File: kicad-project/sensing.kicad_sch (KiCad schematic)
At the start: 10 parts

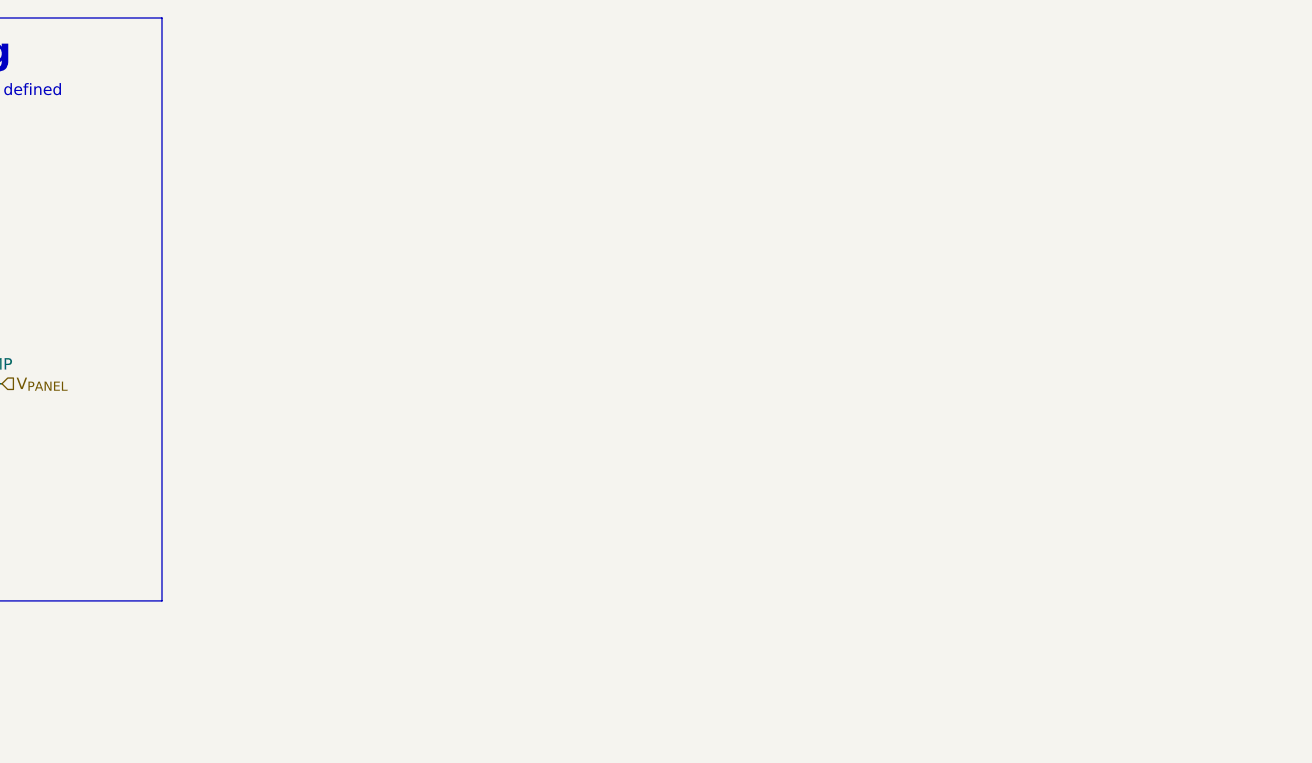
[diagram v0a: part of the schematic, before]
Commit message: fw: added MPU9250
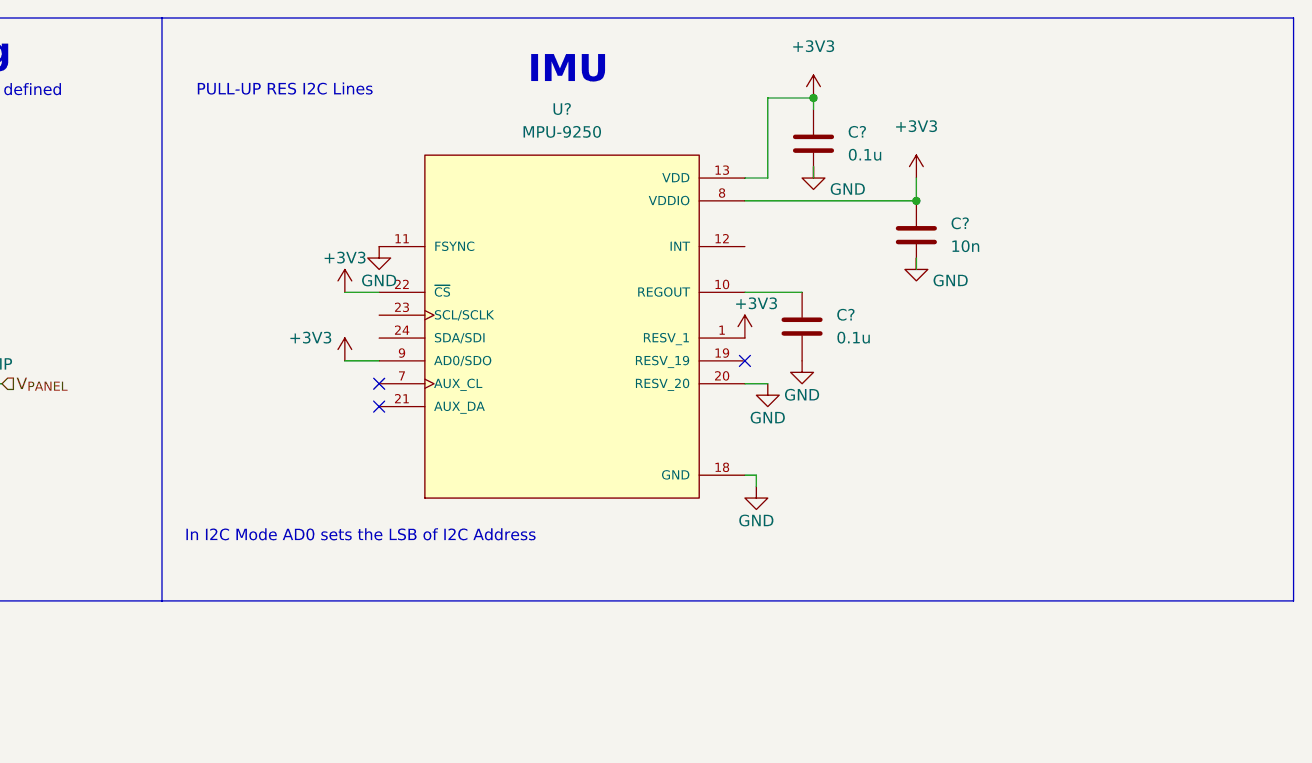
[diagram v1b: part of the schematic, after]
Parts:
- added C? (x2): 0.1u, symbol Device:C
- added C?: 10n, symbol Device:C
- added U?: MPU-9250, QFN40P300X300X105-24N, symbol MPU-9250:MPU-9250
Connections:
- net +3V3: now also C?.1, C?.1, U?.1 (RESV_1), U?.13 (VDD), U?.22 (~{CS}), U?.8 (VDDIO), U?.9 (AD0/SDO)
- net GND: now also C?.2, C?.2, C?.2, U?.11 (FSYNC), U?.18 (GND), U?.20 (RESV_20)
- new net: C?.1, U?.10 (REGOUT)
- no-connect marks 0 -> 3
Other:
- note added: "IMU"
- note added: "In I2C Mode AD0 sets the LSB of I2C Address"
- note added: "PULL-UP RES I2C Lines"

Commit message: hw: add limit switches, dual power input, actuation sheet, debug and expansion connectors and connect sheets
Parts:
- added J? (x2): Conn_01x03, symbol Connector_Generic:Conn_01x03
- C? (x2): value 0.1u -> 100n
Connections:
- net +3V3: now also J?.1 (Pin_1), J?.1 (Pin_1)
- net GND: now also J?.3 (Pin_3), J?.3 (Pin_3)
- net IMU_INT: now reaches U?.12 (INT)
- net I2C_SCL: now reaches U?.23 (SCL/SCLK)
- net I2C_SDA: now reaches U?.24 (SDA/SDI)
- new net LIMIT1: J?.2 (Pin_2)
- new net LIMIT2: J?.2 (Pin_2)
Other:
- note added: "Filter?"
- note added: "Limit switches"

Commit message: hw: schematic updates
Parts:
- removed C? (x2): 100n, symbol Device:C
- removed C?: 10n, symbol Device:C
- removed U?: MPU-9250, QFN40P300X300X105-24N, symbol MPU-9250:MPU-9250
- added D?: (no value), symbol Device:D_Zener
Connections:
- net GND: now also D?.2 (A)
- net at R?.1, R?.2, U?.1 (+): now also D?.1 (K)
- no-connect marks 3 -> 0
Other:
- note removed: "IMU"
- note removed: "In I2C Mode AD0 sets the LSB of I2C Address"
- note removed: "PULL-UP RES I2C Lines"

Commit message: hw: connect filtering capacitor near vdd pin
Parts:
- D?: value (none) -> D_Zener
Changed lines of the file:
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@@
       (effects (font (size 1.27 1.27)) (justify left))
     )
-    (property "Value" "" (id 1) (at 96.52 58.4199 90)
+    (property "Value" "D_Zener" (id 1) (at 96.52 58.4199 90)
       (effects (font (size 1.27 1.27)) (justify left))
     )

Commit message: hw: update schematic pt. 2
add switching enable resistor, change usb inductor to ferrite bead, add OR gate and microstepping solder jumpers to motor driver, remove i2c and backup supply solder jumper from GPS, add ferrite bead to GPS, remove limit switches and other small changes
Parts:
- removed J? (x2): Conn_01x03, symbol Connector_Generic:Conn_01x03
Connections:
- net GND: now also R?.2
- net I_{PANEL}: no longer R?.2
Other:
- note removed: "Filter?"
- note removed: "Limit switches"
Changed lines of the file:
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@@
-    (stroke (width 0) (type default) (color 0 0 0 0))
-  )
-  (polyline (pts (xy 157.48 109.22) (xy 85.598 109.22))
     (stroke (width 0) (type default) (color 0 0 0 0))
   )
@@
     (stroke (width 0) (type default) (color 0 0 0 0))
   )
-  (polyline (pts (xy 157.48 78.74) (xy 157.48 109.22))
-    (stroke (width 0) (type default) (color 0 0 0 0))
-  )
   (wire (pts (xy 104.775 50.8) (xy 104.775 52.07))
     (stroke (width 0) (type default) (color 0 0 0 0))
@@
   )
   (wire (pts (xy 64.77 51.435) (xy 63.5 51.435))
-    (stroke (width 0) (type default) (color 0 0 0 0))
-  )
-  (wire (pts (xy 64.77 35.56) (xy 64.77 51.435))
     (stroke (width 0) (type default) (color 0 0 0 0))
   )
@@
     (effects (font (size 1.27 1.27)) (justify right bottom))
   )
-  (text "Limit switches" (at 104.394 84.836 0)
-    (effects (font (size 3 3) (thickness 0.6) bold) (justify left bottom))
-  )
   (text "Panel connector" (at 33.655 85.725 0)
     (effects (font (size 3 3) (thickness 0.6) bold) (justify left bottom))
   )
-  (text "Filter?" (at 115.57 91.948 0)
-    (effects (font (size 1.27 1.27)) (justify left bottom))
-  )
   (text "OpAmp model needs to be defined" (at 105.41 26.035 0)
     (effects (font (size 1.27 1.27)) (justify left bottom))
@@
     (effects (font (size 1.27 1.27)) (justify right bottom))
   )
-  (hierarchical_label "LIMIT1" (shape output) (at 98.298 97.79 180)
-    (effects (font (size 1.27 1.27)) (justify right))
-  )
   (hierarchical_label "V_{PANEL}" (shape output) (at 142.24 54.61 0)
     (effects (font (size 1.27 1.27)) (justify left))
@@
     (effects (font (size 1.27 1.27)) (justify left))
   )
-  (hierarchical_label "LIMIT2" (shape output) (at 132.08 97.79 180)
-    (effects (font (size 1.27 1.27)) (justify right))
-  )
-  (symbol (lib_id "power:GND") (at 132.08 100.33 0) (unit 1)
-    (in_bom yes) (on_board yes) (fields_autoplaced)
-    (property "Reference" "#PWR?" (id 0) (at 132.08 106.68 0)
-      (effects (font (size 1.27 1.27)) hide)
-    )
-    (property "Value" "GND" (id 1) (at 132.08 105.41 0))
-    (property "Footprint" "" (id 2) (at 132.08 100.33 0)
-      (effects (font (size 1.27 1.27)) hide)
-    )
-    (property "Datasheet" "" (id 3) (at 132.08 100.33 0)
-      (effects (font (size 1.27 1.27)) hide)
-    )
-    (pin "1")
-  )
   (symbol (lib_id "power:GND") (at 104.775 60.96 0) (unit 1)
     (in_bom yes) (on_board yes)
@@
     (pin "1")
   )
-  (symbol (lib_id "Connector_Generic:Conn_01x03") (at 137.16 97.79 0) (unit 1)
-    (in_bom yes) (on_board yes) (fields_autoplaced)
-    (property "Reference" "J?" (id 0) (at 139.192 96.5199 0)
-      (effects (font (size 1.27 1.27)) (justify left))
-    )
-    (property "Value" "Conn_01x03" (id 1) (at 139.192 99.0599 0)
-      (effects (font (size 1.27 1.27)) (justify left))
-    )
-    (property "Footprint" "" (id 2) (at 137.16 97.79 0)
-      (effects (font (size 1.27 1.27)) hide)
-    )
-    (property "Datasheet" "~" (id 3) (at 137.16 97.79 0)
-      (effects (font (size 1.27 1.27)) hide)
-    )
-    (pin "1")
-    (pin "2")
-    (pin "3")
-  )
   (symbol (lib_id "power:+3V3") (at 53.34 43.815 0) (unit 1)
     (in_bom yes) (on_board yes)
@@
     )
     (property "Datasheet" "" (id 3) (at 53.34 43.815 0)
+      (effects (font (size 1.27 1.27)) hide)
+    )
+    (pin "1")
+  )
+  (symbol (lib_id "power:GND") (at 64.77 35.56 0) (unit 1)
+    (in_bom yes) (on_board yes)
+    (property "Reference" "#PWR?" (id 0) (at 64.77 41.91 0)
+      (effects (font (size 1.27 1.27)) hide)
+    )
+    (property "Value" "GND" (id 1) (at 64.77 39.37 0))
+    (property "Footprint" "" (id 2) (at 64.77 35.56 0)
+      (effects (font (size 1.27 1.27)) hide)
+    )
+    (property "Datasheet" "" (id 3) (at 64.77 35.56 0)
       (effects (font (size 1.27 1.27)) hide)
     )
@@
     (pin "2")
   )
-  (symbol (lib_id "power:+3V3") (at 132.08 95.25 0) (unit 1)
-    (in_bom yes) (on_board yes) (fields_autoplaced)
-    (property "Reference" "#PWR?" (id 0) (at 132.08 99.06 0)
-      (effects (font (size 1.27 1.27)) hide)
-    )
-    (property "Value" "+3V3" (id 1) (at 132.08 89.535 0))
-    (property "Footprint" "" (id 2) (at 132.08 95.25 0)
-      (effects (font (size 1.27 1.27)) hide)
-    )
-    (property "Datasheet" "" (id 3) (at 132.08 95.25 0)
-      (effects (font (size 1.27 1.27)) hide)
-    )
-    (pin "1")
-  )
   (symbol (lib_id "Device:R_Shunt") (at 28.575 51.435 0) (unit 1)
     (in_bom yes) (on_board yes) (fields_autoplaced)
@@
     (pin "3")
     (pin "4")
-  )
-  (symbol (lib_id "power:+3V3") (at 98.298 95.25 0) (unit 1)
-    (in_bom yes) (on_board yes) (fields_autoplaced)
-    (property "Reference" "#PWR?" (id 0) (at 98.298 99.06 0)
-      (effects (font (size 1.27 1.27)) hide)
-    )
-    (property "Value" "+3V3" (id 1) (at 98.298 89.535 0))
-    (property "Footprint" "" (id 2) (at 98.298 95.25 0)
-      (effects (font (size 1.27 1.27)) hide)
-    )
-    (property "Datasheet" "" (id 3) (at 98.298 95.25 0)
-      (effects (font (size 1.27 1.27)) hide)
-    )
-    (pin "1")
   )
   (symbol (lib_id "power:+3V3") (at 125.095 46.99 0) (unit 1)
@@
     (pin "2")
   )
-  (symbol (lib_id "power:GND") (at 98.298 100.33 0) (unit 1)
-    (in_bom yes) (on_board yes) (fields_autoplaced)
-    (property "Reference" "#PWR?" (id 0) (at 98.298 106.68 0)
-      (effects (font (size 1.27 1.27)) hide)
-    )
-    (property "Value" "GND" (id 1) (at 98.298 105.41 0))
-    (property "Footprint" "" (id 2) (at 98.298 100.33 0)
-      (effects (font (size 1.27 1.27)) hide)
-    )
-    (property "Datasheet" "" (id 3) (at 98.298 100.33 0)
-      (effects (font (size 1.27 1.27)) hide)
-    )
-    (pin "1")
-  )
-  (symbol (lib_id "Connector_Generic:Conn_01x03") (at 103.378 97.79 0) (unit 1)
-    (in_bom yes) (on_board yes) (fields_autoplaced)
-    (property "Reference" "J?" (id 0) (at 105.41 96.5199 0)
-      (effects (font (size 1.27 1.27)) (justify left))
-    )
-    (property "Value" "Conn_01x03" (id 1) (at 105.41 99.0599 0)
-      (effects (font (size 1.27 1.27)) (justify left))
-    )
-    (property "Footprint" "" (id 2) (at 103.378 97.79 0)
-      (effects (font (size 1.27 1.27)) hide)
-    )
-    (property "Datasheet" "~" (id 3) (at 103.378 97.79 0)
-      (effects (font (size 1.27 1.27)) hide)
-    )
-    (pin "1")
-    (pin "2")
-    (pin "3")
-  )
 )

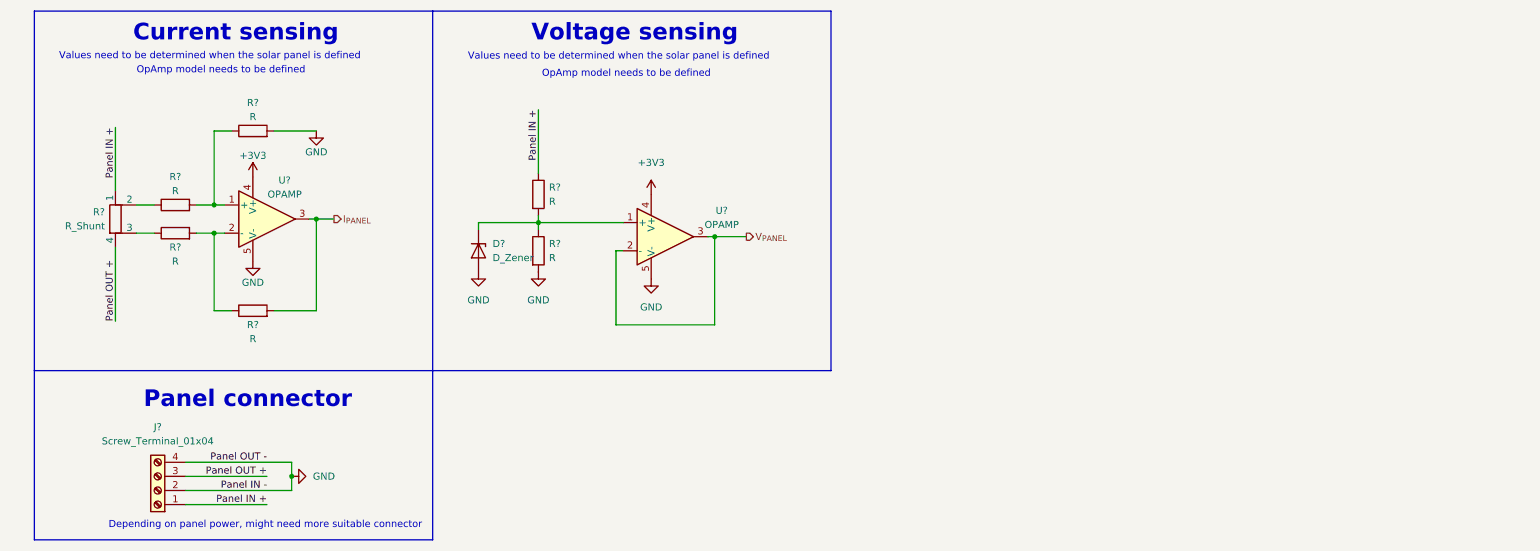
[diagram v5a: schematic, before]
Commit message: hw: set grid to 50 mils and missing labels
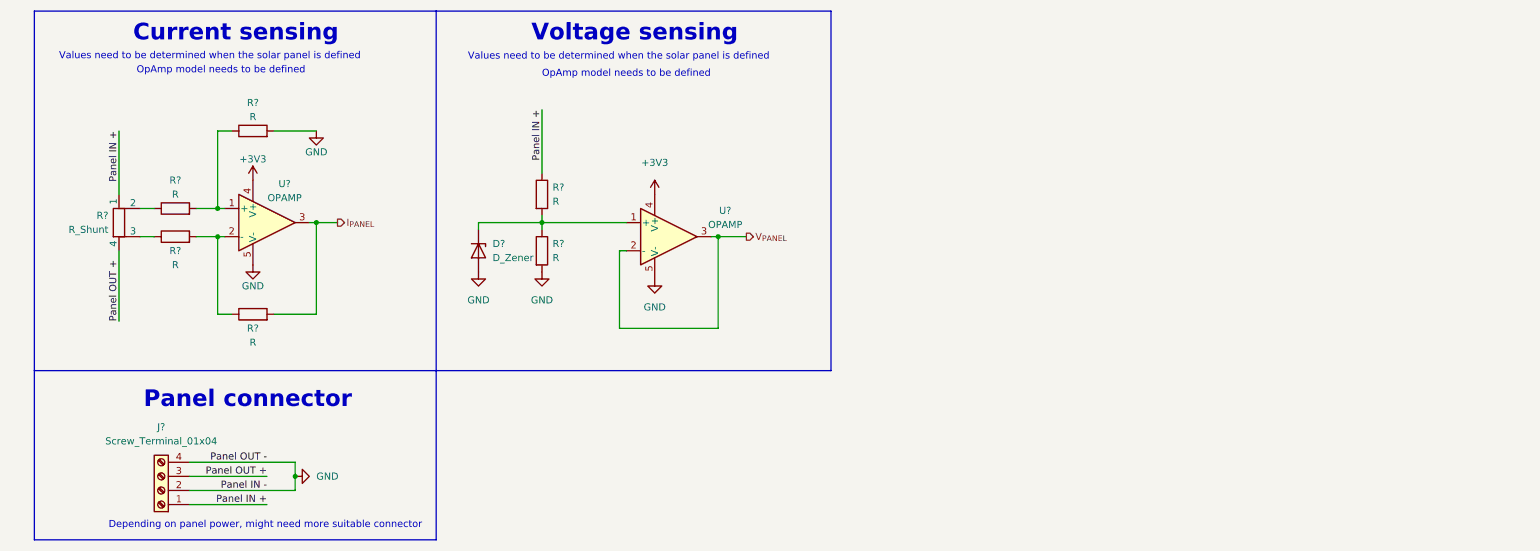
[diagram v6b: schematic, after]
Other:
- moved on the sheet: J?, R?, U?
